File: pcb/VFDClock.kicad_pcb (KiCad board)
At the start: 2 copper layers, 96.5 x 86.4 mm, 16 parts, among them SW1 SW_SPST, SW2 SW_SPST, U4 ESP32-S3-WROOM-1, U5 AMS1117-3.3

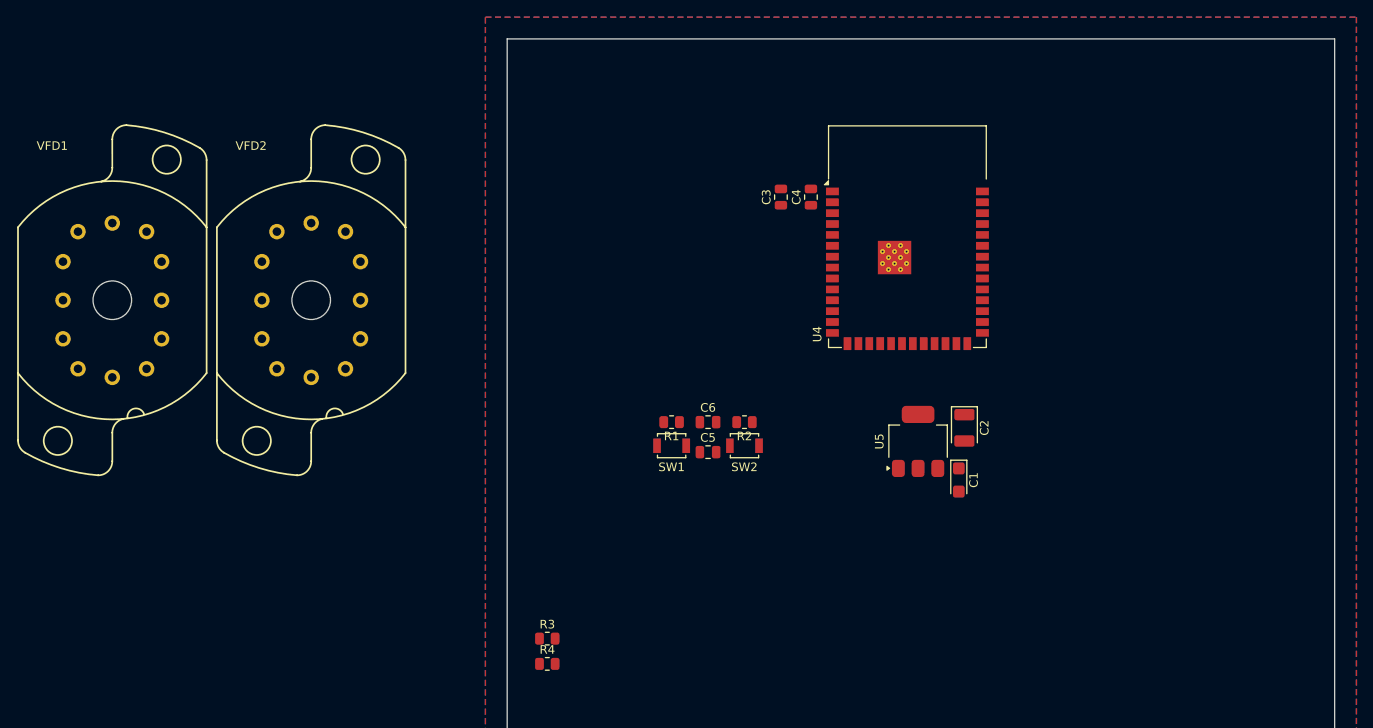
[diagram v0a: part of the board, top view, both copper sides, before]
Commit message: Added linear regulator for filament voltage
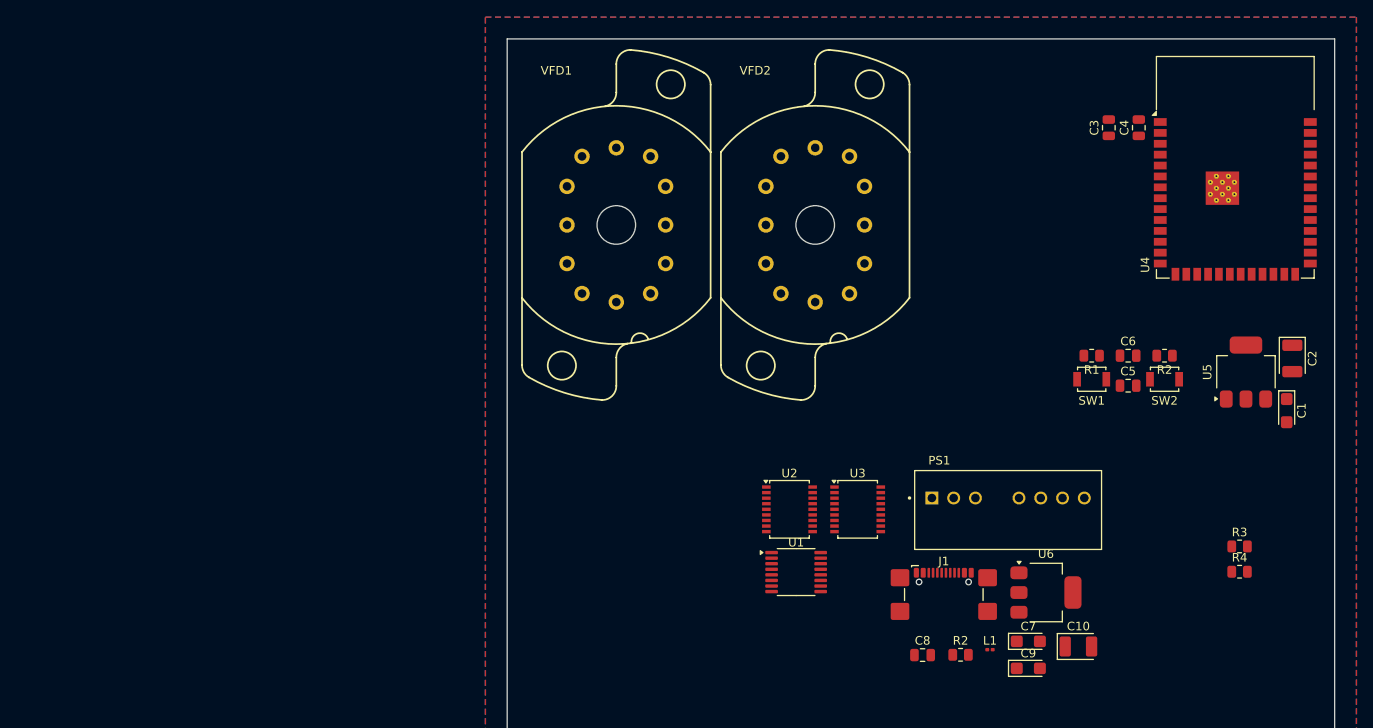
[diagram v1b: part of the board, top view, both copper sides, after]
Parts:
- added C10: 22u, Capacitor_Tantalum_SMD:CP_EIA-3528-15_AVX-H, F.Cu at (150.4, 121.7)
- added C7: 10u, Capacitor_Tantalum_SMD:CP_EIA-3216-18_Kemet-A, F.Cu at (144.6, 121.1)
- added C8: 1u, Capacitor_SMD:C_0805_2012Metric, F.Cu at (132.3, 122.7)
- added C9: 10u, Capacitor_Tantalum_SMD:CP_EIA-3216-18_Kemet-A, F.Cu at (144.6, 124.2)
- added J1: USB_C_Receptacle_USB2.0_16P, Connector_USB:USB_C_Receptacle_GCT_USB4110, F.Cu at (134.8, 116.8)
- added L1: 5.6u, Inductor_SMD:L_0201_0603Metric, F.Cu at (140.1, 122.0)
- added PS1: RS3K-0524S_H3, VFDClock_custom_lib:CONV_RS3K-0524S_H3, F.Cu at (142.2, 105.8)
- added R2: 100, Resistor_SMD:R_0805_2012Metric, F.Cu at (136.7, 122.6)
- added U1: SN74HC595PWR, Package_SO:TSSOP-16_4.4x5mm_P0.65mm, F.Cu at (117.5, 113.0)
- added U2: TBD62783AFNG, Package_SO:SSOP-18_4.4x6.5mm_P0.65mm, F.Cu at (116.8, 105.7)
- added U3: TBD62783AFWG, Package_SO:SSOP-18_4.4x6.5mm_P0.65mm, F.Cu at (124.7, 105.7)
- added U6: AMS1117-1.5, Package_TO_SOT_SMD:SOT-223-3_TabPin2, F.Cu at (146.7, 115.4)
- moved R3 81.5 mm to (169.2, 110.0)
- moved R4 81.5 mm to (169.2, 113.0)
- moved VFD1 59.4 mm to (96.5, 72.5)
- moved VFD2 59.4 mm to (119.8, 72.5)
- moved C5 49.6 mm to (156.2, 91.2)
- moved C6 49.6 mm to (156.2, 87.8)
- moved R1 49.6 mm to (152.0, 87.8)
- moved R2 49.6 mm to (160.5, 87.8)
- moved SW1 49.6 mm to (152.0, 90.5)
- moved SW2 49.6 mm to (160.5, 90.5)
- moved C1 39.1 mm to (174.7, 94.2)
- moved C2 39.1 mm to (175.4, 88.1)
- moved C3 39.1 mm to (154.0, 61.2)
- moved C4 39.1 mm to (157.5, 61.2)
- moved U4 39.1 mm to (168.8, 65.8)
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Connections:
- U4 pad 17: unconnected-(U4-IO9-Pad17) -> /DRIVER_L1
- U4 pad 18: unconnected-(U4-IO10-Pad18) -> /DRIVER_L2
- U4 pad 19: unconnected-(U4-IO11-Pad19) -> /DRIVER_M1
- U4 pad 20: unconnected-(U4-IO12-Pad20) -> /DRIVER_M2
- U4 pad 21: unconnected-(U4-IO13-Pad21) -> /DRIVER_R1
- U4 pad 22: unconnected-(U4-IO14-Pad22) -> /DRIVER_R2
- U4 pad 23: unconnected-(U4-IO21-Pad23) -> /SER_LEFT
- U4 pad 24: unconnected-(U4-IO47-Pad24) -> /SER_RIGHT
- U4 pad 28: unconnected-(U4-IO35-Pad28) -> /SRCLK
- U4 pad 29: unconnected-(U4-IO36-Pad29) -> //SRCLR
- U4 pad 30: unconnected-(U4-IO37-Pad30) -> /RCLK
- U4 pad 31: unconnected-(U4-IO38-Pad31) -> /SER_MID

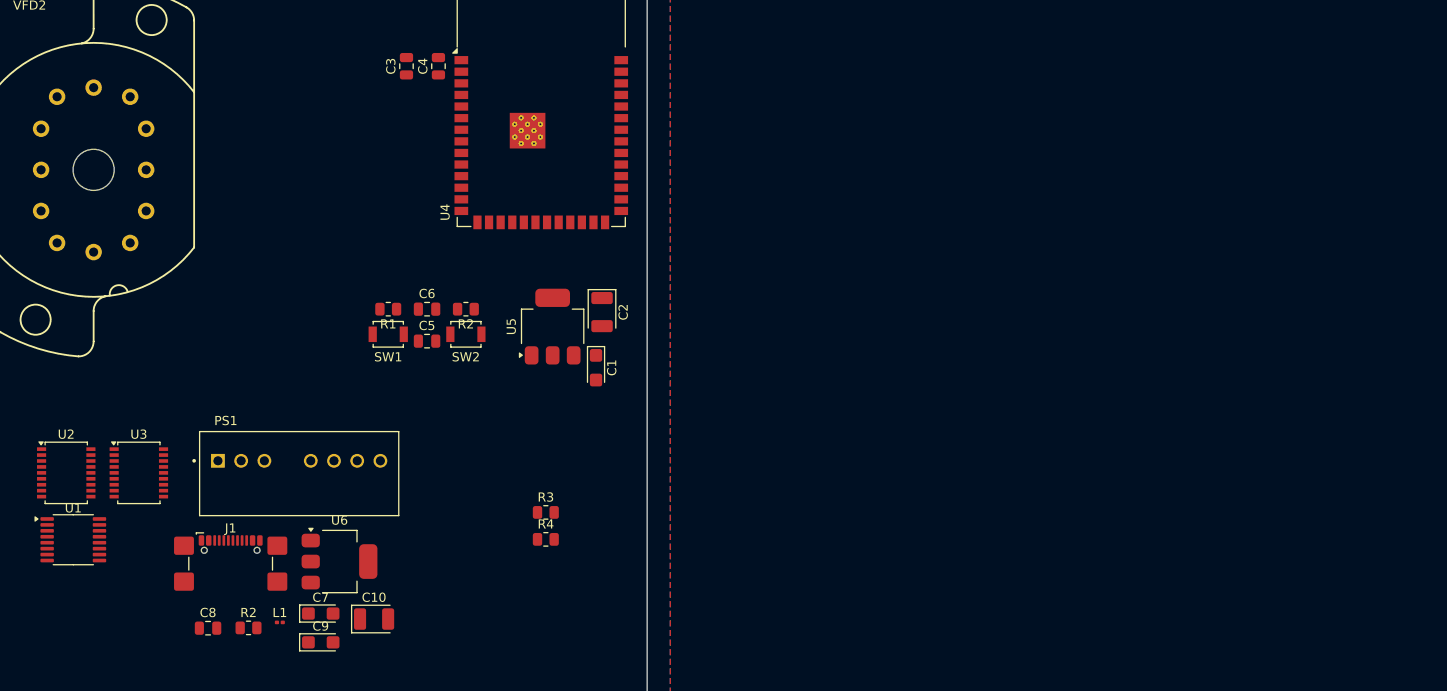
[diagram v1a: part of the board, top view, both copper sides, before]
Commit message: Added TVS and packages for components
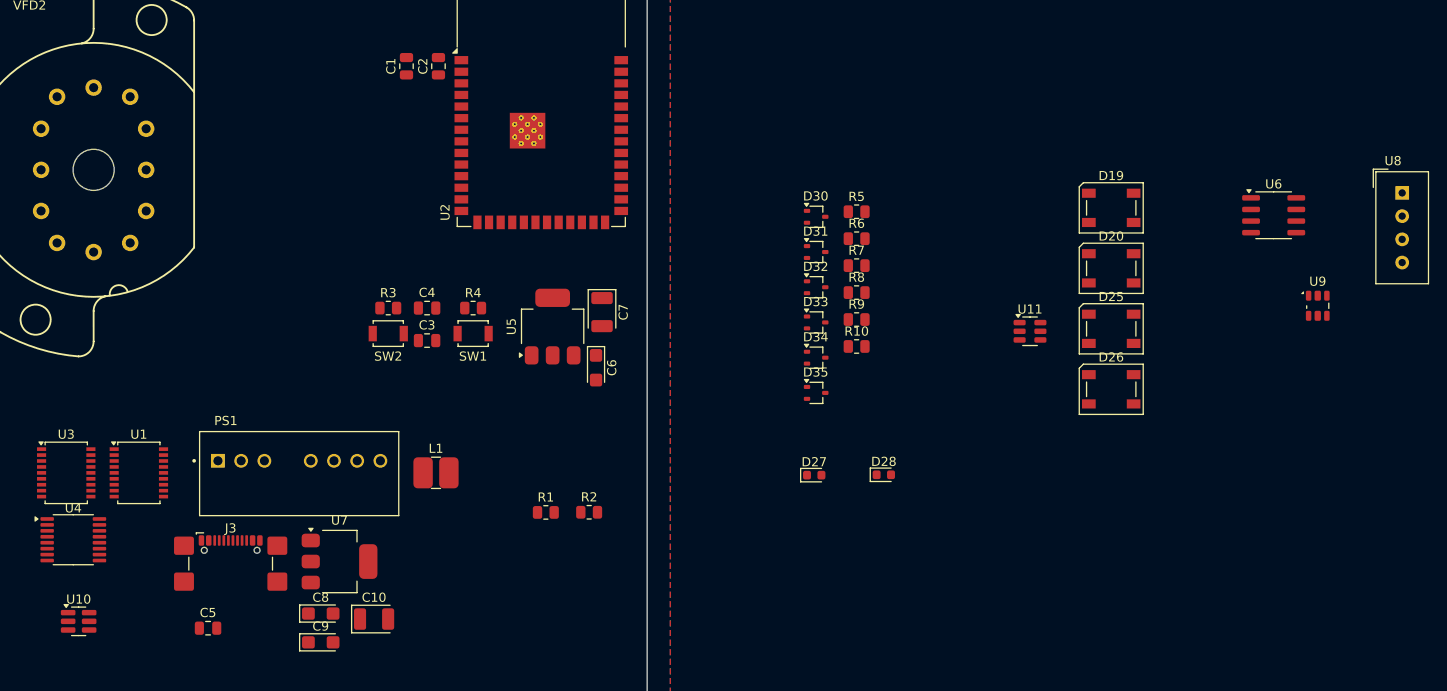
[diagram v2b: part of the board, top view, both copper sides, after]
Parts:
- removed the R2 at (160.5, 87.8)
- removed the SW2 at (160.5, 90.5)
- added D19: Inolux_IN-PI554FCH, LED_SMD:LED_Inolux_IN-PI554FCH_PLCC4_5.0x5.0mm_P3.2mm, F.Cu at (231.1, 76.7)
- added D20: Inolux_IN-PI554FCH, LED_SMD:LED_Inolux_IN-PI554FCH_PLCC4_5.0x5.0mm_P3.2mm, F.Cu at (231.1, 83.3)
- added D25: Inolux_IN-PI554FCH, LED_SMD:LED_Inolux_IN-PI554FCH_PLCC4_5.0x5.0mm_P3.2mm, F.Cu at (231.1, 89.9)
- added D26: Inolux_IN-PI554FCH, LED_SMD:LED_Inolux_IN-PI554FCH_PLCC4_5.0x5.0mm_P3.2mm, F.Cu at (231.1, 96.5)
- added D27: Power LED, Diode_SMD:D_0603_1608Metric, F.Cu at (198.6, 105.9)
- added D28: MCU LED, LED_SMD:LED_0603_1608Metric, F.Cu at (206.2, 105.9)
- added D30: 1PS70SB84, Package_TO_SOT_SMD:SOT-323_SC-70, F.Cu at (198.8, 77.6)
- added D31: 1PS70SB84, Package_TO_SOT_SMD:SOT-323_SC-70, F.Cu at (198.8, 81.5)
- added D32: 1PS70SB84, Package_TO_SOT_SMD:SOT-323_SC-70, F.Cu at (198.8, 85.3)
- added D33: 1PS70SB84, Package_TO_SOT_SMD:SOT-323_SC-70, F.Cu at (198.8, 89.2)
- added D34: 1PS70SB84, Package_TO_SOT_SMD:SOT-323_SC-70, F.Cu at (198.8, 93.1)
- added D35: 1PS70SB84, Package_TO_SOT_SMD:SOT-323_SC-70, F.Cu at (198.8, 96.9)
- added R10: 180, Resistor_SMD:R_0805_2012Metric, F.Cu at (203.3, 91.8)
- added R5: 10k, Resistor_SMD:R_0805_2012Metric, F.Cu at (203.3, 77.1)
- added R6: 10k, Resistor_SMD:R_0805_2012Metric, F.Cu at (203.3, 80.0)
- added R7: 10k, Resistor_SMD:R_0805_2012Metric, F.Cu at (203.3, 83.0)
- added R8: 10k, Resistor_SMD:R_0805_2012Metric, F.Cu at (203.3, 85.9)
- added R9: 180, Resistor_SMD:R_0805_2012Metric, F.Cu at (203.3, 88.9)
- added SW1: SW_SPST, Button_Switch_SMD:SW_SPST_B3U-1000P, F.Cu at (161.3, 90.4)
- added U10: IP4234CZ6, Package_TO_SOT_SMD:SC-74-6_1.55x2.9mm_P0.95mm, F.Cu at (118.1, 121.9)
- added U11: TXS0101DBV, Package_TO_SOT_SMD:SOT-23-6, F.Cu at (222.2, 90.2)
- added U6: BQ32000, Package_SO:SOIC-8_3.9x4.9mm_P1.27mm, F.Cu at (248.9, 77.5)
- added U8: DHT11, Sensor:Aosong_DHT11_5.5x12.0_P2.54mm, F.Cu at (263.0, 75.0)
- added U9: APDS-9301, OptoDevice:Broadcom_APDS-9301, F.Cu at (253.7, 87.4)
- L1: footprint Inductor_SMD:L_0201_0603Metric -> Inductor_SMD:L_1812_4532Metric
- R4: renamed from R2; value 100 -> 10k
- moved R4 42.8 mm to (161.3, 87.6)
- moved L1 23.7 mm to (157.2, 105.7)
- moved R2 5.59 mm to (174.0, 110.0)
- moved C4 0.12 mm to (156.2, 87.6)
- moved R3 0.12 mm to (152.0, 87.6), turned to 0 degrees
- moved SW2 0.08 mm to (152.0, 90.4)
- moved C3 0.06 mm to (156.2, 91.2)
- renumbered C3 to C1, C4 to C2, C5 to C3, C6 to C4, C8 to C5, C1 to C6, C2 to C7, C7 to C8, J1 to J3, R3 to R1, R4 to R2, R1 to R3, SW1 to SW2, U3 to U1, U4 to U2, U2 to U3, U1 to U4, U6 to U7
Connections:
- J3 pad A6: /USB_D_DP -> Net-(J3-D+-PadA6)
- J3 pad A7: /USB_D_DN -> Net-(J3-D--PadA7)
- J3 pad B6: /USB_D_DP -> Net-(J3-D+-PadA6)
- J3 pad B7: /USB_D_DN -> Net-(J3-D--PadA7)
- U2 pad 10: unconnected-(U4-IO17-Pad10) -> /SCL
- U2 pad 11: unconnected-(U4-IO18-Pad11) -> /SDA
- U2 pad 12: unconnected-(U4-IO8-Pad12) -> /BTN4
- U2 pad 32: unconnected-(U4-IO39-Pad32) -> /TEMP_DATA
- U2 pad 38: unconnected-(U4-IO2-Pad38) -> /LED2
- U2 pad 39: unconnected-(U4-IO1-Pad39) -> /LED1
- U2 pad 4: unconnected-(U4-IO4-Pad4) -> /COLON_LED
- U2 pad 5: unconnected-(U4-IO5-Pad5) -> /BTN1
- U2 pad 6: unconnected-(U4-IO6-Pad6) -> /BTN2
- U2 pad 7: unconnected-(U4-IO7-Pad7) -> /BTN3
- U2 pad 8: unconnected-(U4-IO15-Pad8) -> /RTC_SCL
- U2 pad 9: unconnected-(U4-IO16-Pad9) -> /RTC_SDA
